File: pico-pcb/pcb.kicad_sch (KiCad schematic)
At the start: 24 parts, among them J1 AudioJack1, J2 AudioJack2, Q1 2N3904, SW1 SW_DIP_x04, U1 Pico

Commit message: Updated schematic with new pinning on trrs jack to make it digirig cable compatible.
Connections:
- net MIC: now also J1.R1; no longer J1.T
- net SP: now also J1.T; no longer J1.R1
- net PSAVE renamed OPT2
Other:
- note added: "R9 Yaesu 4.7K Standard 22k Icom 22k"
- note removed: "R6 Yaesu 4.7K Standard 22k Icom 22k"

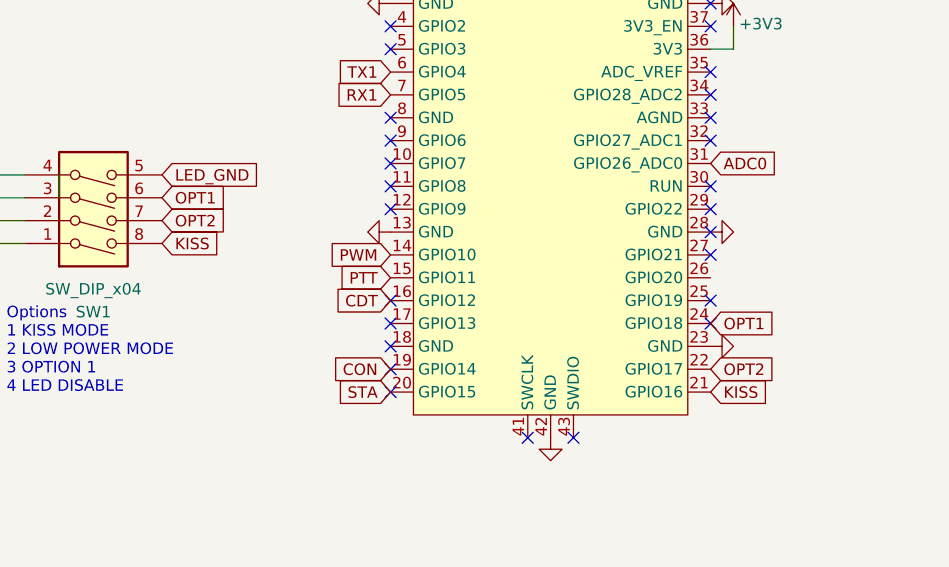
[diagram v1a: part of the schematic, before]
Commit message: modified name of dip switch inputs
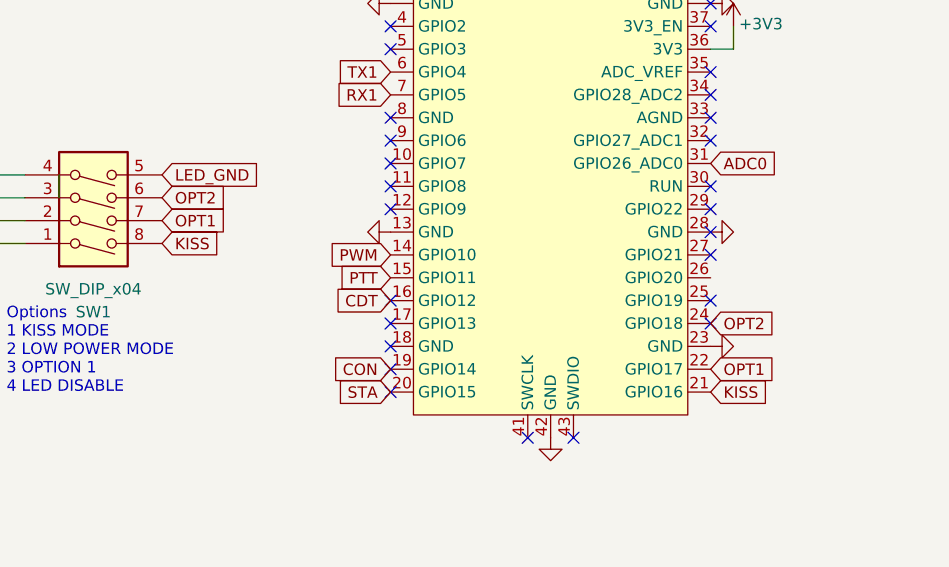
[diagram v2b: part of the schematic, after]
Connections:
- net OPT1: now also SW1.7, U1.22 (GPIO17); no longer SW1.6, U1.24 (GPIO18)
- net OPT2: now also SW1.6, U1.24 (GPIO18); no longer SW1.7, U1.22 (GPIO17)
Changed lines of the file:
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@@
 	(global_label "OPT2"
 		(shape input)
-		(at 41.91 107.95 0)
-		(fields_autoplaced yes)
-		(effects
-			(font
-				(size 1.27 1.27)
-			)
-			(justify left)
-		)
-		(property "Intersheetrefs" "${INTERSHEET_REFS}"
-			(at 49.6728 107.95 0)
+		(at 41.91 105.41 0)
+		(fields_autoplaced yes)
+		(effects
+			(font
+				(size 1.27 1.27)
+			)
+			(justify left)
+		)
+		(property "Intersheetrefs" "${INTERSHEET_REFS}"
+			(at 49.6728 105.41 0)
 			(effects
 				(font
@@
 	(global_label "OPT1"
 		(shape input)
-		(at 41.91 105.41 0)
-		(fields_autoplaced yes)
-		(effects
-			(font
-				(size 1.27 1.27)
-			)
-			(justify left)
-		)
-		(property "Intersheetrefs" "${INTERSHEET_REFS}"
-			(at 49.6728 105.41 0)
+		(at 41.91 107.95 0)
+		(fields_autoplaced yes)
+		(effects
+			(font
+				(size 1.27 1.27)
+			)
+			(justify left)
+		)
+		(property "Intersheetrefs" "${INTERSHEET_REFS}"
+			(at 49.6728 107.95 0)
 			(effects
 				(font
@@
 	(global_label "OPT2"
 		(shape input)
+		(at 102.87 119.38 0)
+		(fields_autoplaced yes)
+		(effects
+			(font
+				(size 1.27 1.27)
+			)
+			(justify left)
+		)
+		(property "Intersheetrefs" "${INTERSHEET_REFS}"
+			(at 110.6328 119.38 0)
+			(effects
+				(font
+					(size 1.27 1.27)
+				)
+				(justify left)
+				(hide yes)
+			)
+		)
+	)
+	(global_label "CDT"
+		(shape input)
+		(at 143.51 110.49 180)
+		(fields_autoplaced yes)
+		(effects
+			(font
+				(size 1.27 1.27)
+			)
+			(justify right)
+		)
+		(property "Intersheetrefs" "${INTERSHEET_REFS}"
+			(at 137.0172 110.49 0)
+			(effects
+				(font
+					(size 1.27 1.27)
+				)
+				(justify right)
+				(hide yes)
+			)
+		)
+	)
+	(global_label "OPT1"
+		(shape input)
 		(at 102.87 124.46 0)
 		(fields_autoplaced yes)
@@
 			(effects
 				(font
-					(size 1.27 1.27)
-				)
-				(justify left)
-				(hide yes)
-			)
-		)
-	)
-	(global_label "CDT"
-		(shape input)
-		(at 143.51 110.49 180)
-		(fields_autoplaced yes)
-		(effects
-			(font
-				(size 1.27 1.27)
-			)
-			(justify right)
-		)
-		(property "Intersheetrefs" "${INTERSHEET_REFS}"
-			(at 137.0172 110.49 0)
-			(effects
-				(font
-					(size 1.27 1.27)
-				)
-				(justify right)
-				(hide yes)
-			)
-		)
-	)
-	(global_label "OPT1"
-		(shape input)
-		(at 102.87 119.38 0)
-		(fields_autoplaced yes)
-		(effects
-			(font
-				(size 1.27 1.27)
-			)
-			(justify left)
-		)
-		(property "Intersheetrefs" "${INTERSHEET_REFS}"
-			(at 110.6328 119.38 0)
-			(effects
-				(font

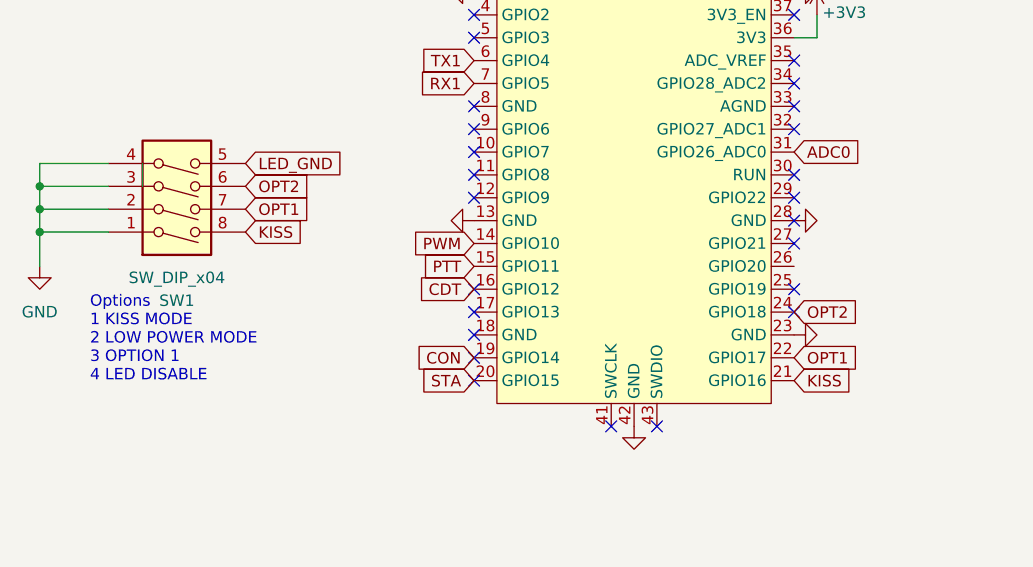
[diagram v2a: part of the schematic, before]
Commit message: Modified schematic to reflect dip switch labels
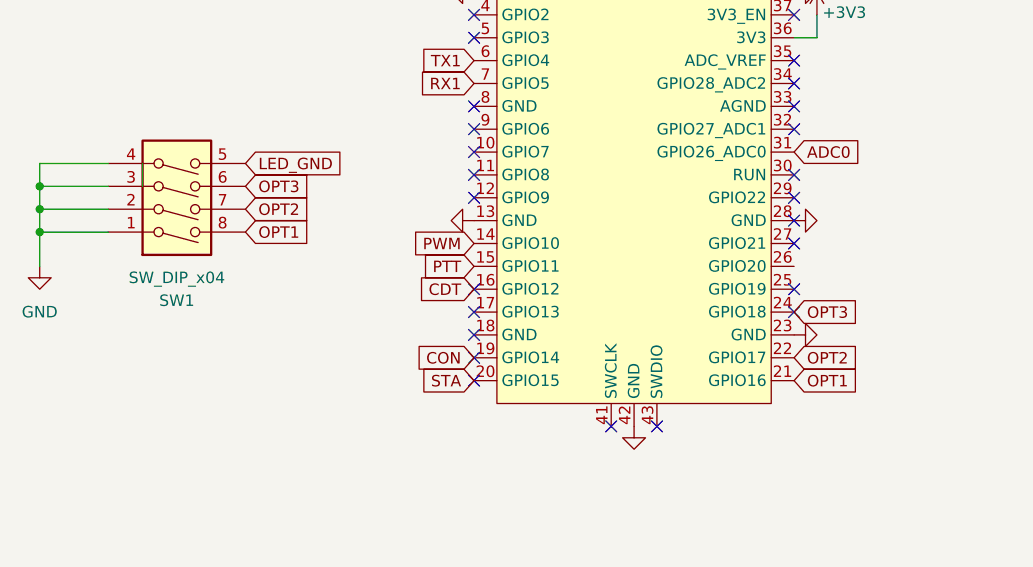
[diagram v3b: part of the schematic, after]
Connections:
- net KISS is gone; now on net OPT1: SW1.8, U1.21 (GPIO16)
- net OPT1: no longer SW1.7, U1.22 (GPIO17)
- net OPT2: now also SW1.7, U1.22 (GPIO17); no longer SW1.6, U1.24 (GPIO18)
- new net OPT3: SW1.6, U1.24 (GPIO18)
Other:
- note removed: "Options 1 KISS MODE 2 LOW POWER MODE 3 OPTION 1 4 LED DISABLE"

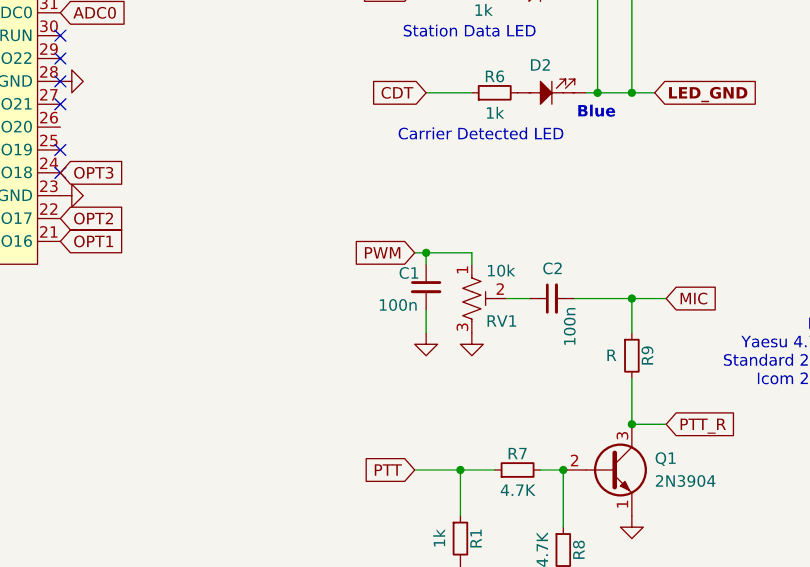
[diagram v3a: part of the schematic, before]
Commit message: Updated Schematic and PCB to add 100ohm resistor to pwm circuit as per original pico tnc and recommendation by Mario AE0GL
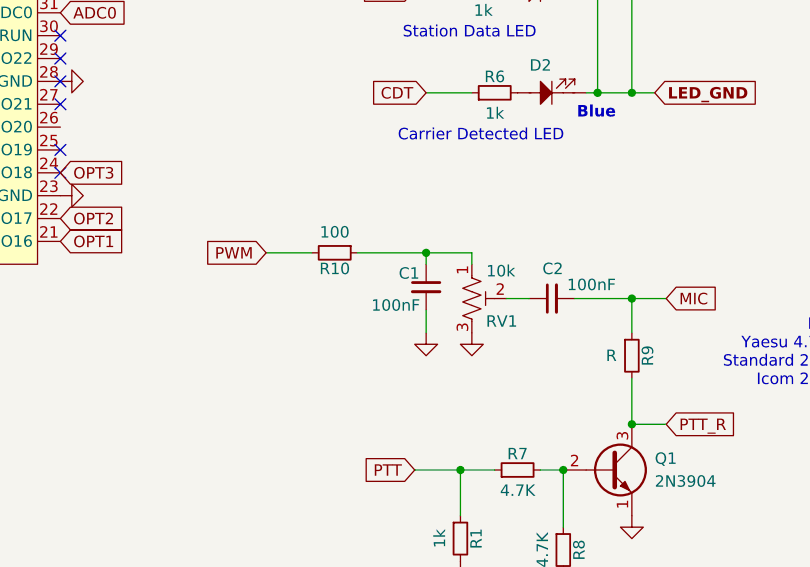
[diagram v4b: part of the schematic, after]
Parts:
- added R10: 100, Resistor_THT:R_Axial_DIN0204_L3.6mm_D1.6mm_P5.08mm_Horizontal, symbol Device:R_Small
- C1, C2: value 100n -> 100nF
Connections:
- net PWM: now also R10.2; no longer C1.1, RV1.1
- new net: C1.1, R10.1, RV1.1
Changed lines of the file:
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@@
 	(title_block
 		(title "Pico TncEmu Radio Interface SubBoard")
-		(date "2025-08-13")
-		(rev "0.01")
+		(date "2025-11-18")
+		(rev "0.70")
 		(company "pfiliberti (KF7PSM)")
 	)
@@
 	(wire
 		(pts
+			(xy 135.89 128.27) (xy 143.51 128.27)
+		)
+		(stroke
+			(width 0)
+			(type default)
+		)
+	)
+	(wire
+		(pts
 			(xy 142.24 88.9) (xy 147.32 88.9)
 		)
@@
 	(wire
 		(pts
+			(xy 125.73 128.27) (xy 130.81 128.27)
+		)
+		(stroke
+			(width 0)
+			(type default)
+		)
+	)
+	(wire
+		(pts
 			(xy 149.86 66.04) (xy 149.86 68.58)
 		)
@@
 	(wire
 		(pts
-			(xy 142.24 128.27) (xy 143.51 128.27)
-		)
-		(stroke
-			(width 0)
-			(type default)
-		)
-	)
-	(wire
-		(pts
 			(xy 142.24 152.4) (xy 147.32 152.4)
 		)
@@
 	(global_label "PWM"
 		(shape input)
-		(at 142.24 128.27 180)
+		(at 125.73 128.27 180)
 		(fields_autoplaced yes)
 		(effects
@@
 		)
 		(property "Intersheetrefs" "${INTERSHEET_REFS}"
-			(at 135.082 128.27 0)
+			(at 118.572 128.27 0)
 			(effects
 				(font
@@
 	(symbol
 		(lib_id "Device:R_Small")
+		(at 133.35 128.27 270)
+		(unit 1)
+		(exclude_from_sim no)
+		(in_bom yes)
+		(on_board yes)
+		(dnp no)
+		(property "Reference" "R10"
+			(at 133.35 130.048 90)
+			(effects
+				(font
+					(size 1.27 1.27)
+				)
+			)
+		)
+		(property "Value" "100"
+			(at 133.35 125.984 90)
+			(effects
+				(font
+					(size 1.27 1.27)
+				)
+			)
+		)
+		(property "Footprint" "Resistor_THT:R_Axial_DIN0204_L3.6mm_D1.6mm_P5.08mm_Horizontal"
+			(at 133.35 128.27 0)
+			(effects
+				(font
+					(size 1.27 1.27)
+				)
+				(hide yes)
+			)
+		)
+		(property "Datasheet" "~"
+			(at 133.35 128.27 0)
+			(effects
+				(font
+					(size 1.27 1.27)
+				)
+				(hide yes)
+			)
+		)
+		(property "Description" "Resistor, small symbol"
+			(at 133.35 128.27 0)
+			(effects
+				(font
+					(size 1.27 1.27)
+				)
+				(hide yes)
+			)
+		)
+		(pin "2"
+		)
+		(pin "1"
+		)
+		(instances
+			(project "pcb"
+				(path "/96a10117-2309-4a27-a12f-47eb48e845e4"
+					(reference "R10")
+					(unit 1)
+				)
+			)
+		)
+	)
+	(symbol
+		(lib_id "Device:R_Small")
 		(at 166.37 139.7 0)
 		(unit 1)
@@
 			)
 		)
-		(property "Value" "100n"
-			(at 159.512 138.684 0)
+		(property "Value" "100nF"
+			(at 164.592 131.826 90)
 			(effects
 				(font
@@
 			)
 		)
-		(property "Value" "100n"
-			(at 138.176 134.112 0)
+		(property "Value" "100nF"
+			(at 137.414 134.112 0)
 			(effects
 				(font
